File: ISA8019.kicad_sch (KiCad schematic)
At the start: 56 parts

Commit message: Add header to switch between SRAM and EPROM
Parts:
- added J11: EPROM/SRAM Selection, Connector_PinHeader_2.54mm:PinHeader_2x03_P2.54mm_Vertical, symbol Connector_Generic:Conn_02x03_Odd_Even
- C1, C12, C15, C3, C4, C5, C6, C7: value (none) -> 100n; footprint (none) -> Capacitor_THT:C_Disc_D6.0mm_W2.5mm_P5.00mm
- C10, C11, C13, C14: value (none) -> 1nF; footprint (none) -> Capacitor_THT:C_Disc_D6.0mm_W2.5mm_P5.00mm
- C16, C2: value (none) -> 10uF; footprint (none) -> Capacitor_THT:CP_Radial_D5.0mm_P2.50mm
- C8, C9: value (none) -> 20p; footprint (none) -> Capacitor_THT:C_Disc_D5.0mm_W2.5mm_P2.50mm
- FB1: value (none) -> Filter; footprint (none) -> Inductor_THT:L_Axial_L5.3mm_D2.2mm_P10.16mm_Horizontal_Vishay_IM-1
- H3, H4: value (none) -> MountingHole_Pad; footprint (none) -> MountingHole:MountingHole_3.2mm_M3_Pad_Via
- J1: value (none) -> Bus_ISA_8bit; footprint (none) -> My_Components:Conn_Edge_PCB_ISA8
- J10: value (none) -> Extra Address Lines; footprint (none) -> Connector_PinHeader_2.54mm:PinHeader_1x03_P2.54mm_Vertical
- J2: value (none) -> 8P8C_Shielded; footprint (none) -> Connector_Ethernet:8P8C_yellow_green_Ckmtw_C133529
- J4: value (none) -> Jumper mode; footprint (none) -> Connector_PinHeader_2.54mm:PinHeader_2x01_P2.54mm_Vertical
- J5: value (none) -> PNP force; footprint (none) -> Connector_PinHeader_2.54mm:PinHeader_2x01_P2.54mm_Vertical
- J6: value (none) -> BROM size and base address; footprint (none) -> Connector_PinHeader_2.54mm:PinHeader_2x05_P2.54mm_Vertical
- J7: value (none) -> I/O base address; footprint (none) -> Connector_PinHeader_2.54mm:PinHeader_2x04_P2.54mm_Vertical
- J8: value (none) -> Medium type; footprint (none) -> Connector_PinHeader_2.54mm:PinHeader_2x02_P2.54mm_Vertical
- J9: value (none) -> IRQ Select; footprint (none) -> Connector_PinHeader_2.54mm:PinHeader_2x03_P2.54mm_Vertical
- R10, R11, R12, R13, R14, R15, R16, R17, R18, R19, R20, R21, R22, R6, R7, R8, R9: value (none) -> 10k; footprint (none) -> Resistor_THT:R_Axial_DIN0207_L6.3mm_D2.5mm_P10.16mm_Horizontal
- R2: value (none) -> 1M; footprint (none) -> Resistor_THT:R_Axial_DIN0207_L6.3mm_D2.5mm_P10.16mm_Horizontal
- R3: value (none) -> 200; footprint (none) -> Resistor_THT:R_Axial_DIN0207_L6.3mm_D2.5mm_P10.16mm_Horizontal
- R4, R5: value (none) -> 1k; footprint (none) -> Resistor_THT:R_Axial_DIN0207_L6.3mm_D2.5mm_P10.16mm_Horizontal
- T1: value (none) -> 13F-39MNL; footprint (none) -> Package_SO:SOIC-16W-12_7.5x10.3mm_P1.27mm
- U1: value (none) -> RTL8019AS; footprint (none) -> Package_QFP_Realtek:LQFP-14x20mm_P0.5mm
- U2: value (none) -> AT93C46DN; footprint (none) -> Package_SO:SOIC-8_3.9x4.9mm_P1.27mm
- U3: value (none) -> SST39SF040; footprint (none) -> Package_DIP:DIP-32_W15.24mm_Socket
- Y1: value (none) -> 20Mhz; footprint (none) -> Crystal:Crystal_HC49-4H_Vertical
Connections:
- net BA14: now also J11.1 (Pin_1), J11.2 (Pin_2); no longer U3.29 (A14)
- net ~{ISA_SMEMW}: now also J11.5 (Pin_5), J11.6 (Pin_6); no longer U3.31 (PGM)
- new net EPROM_A14: J11.3 (Pin_3), U3.29 (A14)
- new net EPROM_PGM: J11.4 (Pin_4), U3.31 (PGM)

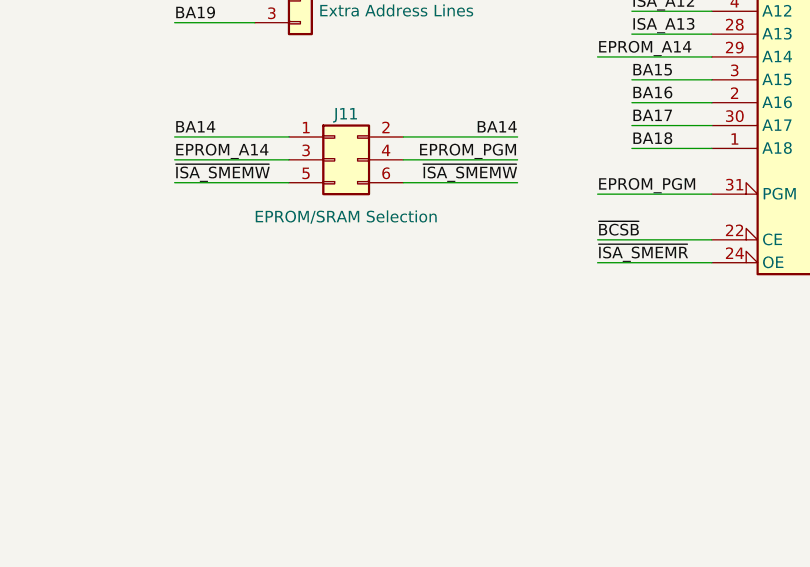
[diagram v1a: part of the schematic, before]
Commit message: Add some descriptive text for J11
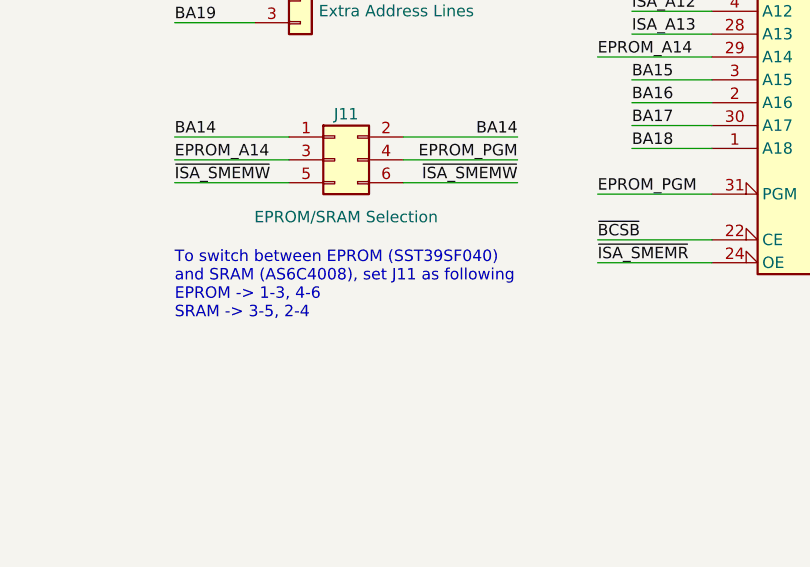
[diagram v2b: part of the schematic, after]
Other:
- note added: "To switch between EPROM (SST39SF040) and SRAM (AS6C4008), set J11 as following EPROM -> 1-3, 4-6 SRAM -> 3-5, 2-4"
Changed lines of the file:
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@@
     (effects (font (size 5.0038 5.0038)) (justify left bottom))
+  )
+  (text "To switch between EPROM (SST39SF040)\nand SRAM (AS6C4008), set J11 as following\nEPROM -> 1-3, 4-6\nSRAM -> 3-5, 2-4"
+    (at 247.65 99.06 0)
+    (effects (font (size 1.27 1.27)) (justify left bottom))
   )
   (text "Base-T Interface" (at 299.72 182.88 0)
